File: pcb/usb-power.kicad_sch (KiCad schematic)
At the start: 10 parts, among them J2 USB4110-GF-A, U9 AP2112K-3.3

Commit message: Lower sense resistance (0.5 -> 0.43 Ohms)
Also:
- Route TMC2130 diagnostic pins to RP2040
- Instead of manually excluding violations:
  - Changed spoke minimum: 2 -> 1
  - Changed copper-to-hole clearance: 0.25mm -> 0.19mm
- Update revision labels on sch, pcb, and silkscreen
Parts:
- J2: footprint open-ephys:USB_C_Receptacle_GCT_USB4110 -> open-ephys:GCT-USB_C_Receptacle_GCT_USB4110
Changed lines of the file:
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@@
 			)
 		)
-		(property "Footprint" "open-ephys:USB_C_Receptacle_GCT_USB4110"
+		(property "Footprint" "open-ephys:GCT-USB_C_Receptacle_GCT_USB4110"
 			(at 109.22 95.25 0)
 			(effects

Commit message: Skip revision I; Fix Board Setup
- Revision labels I -> J
  - Revision I is skipped per ASME standards
- Revert copper-to-hole clearance: 0.19mm ->0.25mm
  - DRC violations resolved with by adding creating a component
    class for USB connector and a custom rule
- Revert minimum thermal relief spoke count: 1 -> 2
  -  DRC violations resolved by manually routing traces
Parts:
- J2: Component Class (none) -> USB
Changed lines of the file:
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@@
+			)
+		)
+		(property "Component Class" "USB"
+			(at 105.41 95.25 0)
+			(effects
+				(font
+					(size 1.27 1.27)
+				)
+				(hide yes)
 			)
 		)

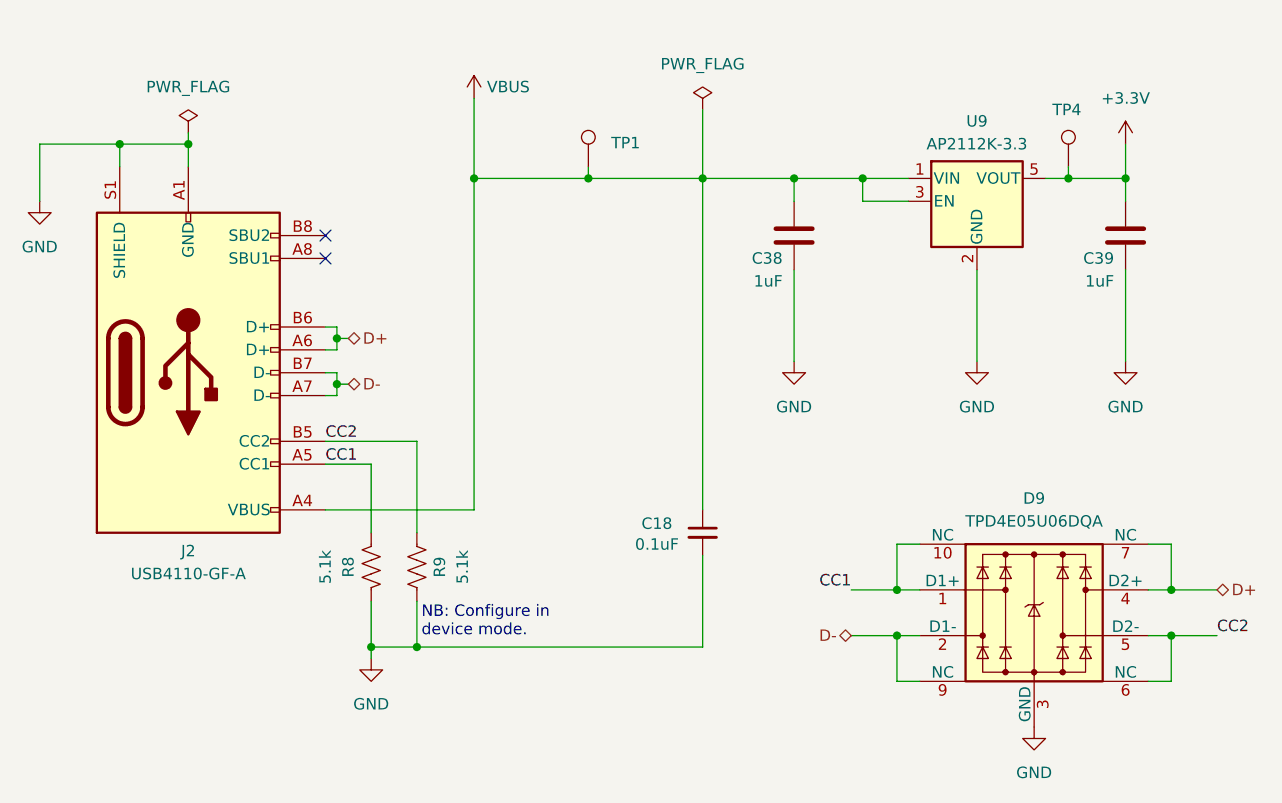
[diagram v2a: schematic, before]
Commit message: Small updates during review
- Schematic clarifications
- Update footprints to match library latest
- Small silkscreen and via positioning changes to support clean
  silkscreen
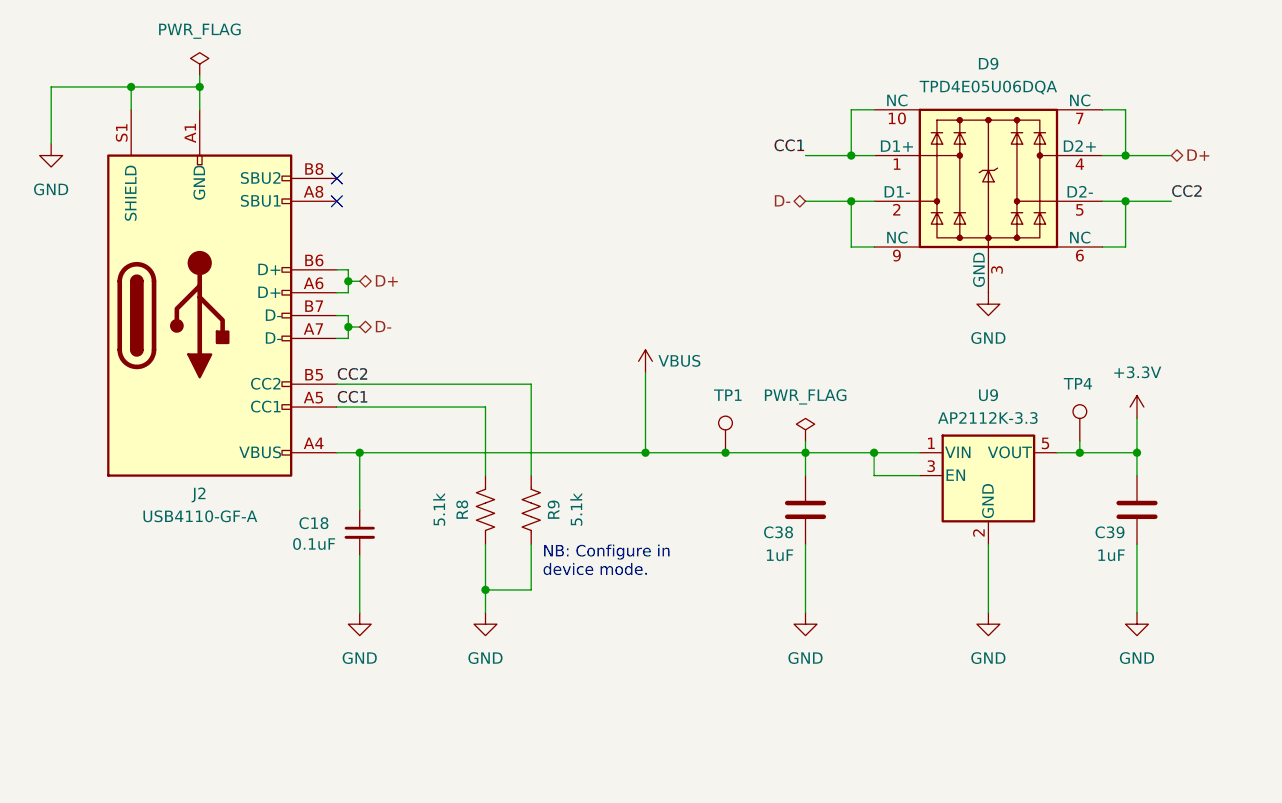
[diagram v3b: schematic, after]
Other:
- moved on the sheet: C18, C38, C39, D9, J2, R8, R9, TP1, TP4, U9
